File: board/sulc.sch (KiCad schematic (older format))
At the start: 66 parts, among them J1 LED_PWR, J2 HWB, P1 USB, P10 CONN_1, P11 CONN_1, P12 CONN_1, P13 CONN_1, P14 CONN_1, P15 CONN_1, P16 CONN_1, P17 CONN_1, P18 CONN_1, P19 CONN_1, P2 CONN_1, P20 CONN_1, P21 CONN_1, P22 CONN_1, P23 CONN_1, P24 CONN_1, P25 CONN_1, P3 CONN_1, P4 CONN_1, P5 CONN_1, P6 CONN_1, P7 ISP, P8 CONN_1, P9 CONN_1, U1 ATMEGA8U2AU, Y1 16MHz

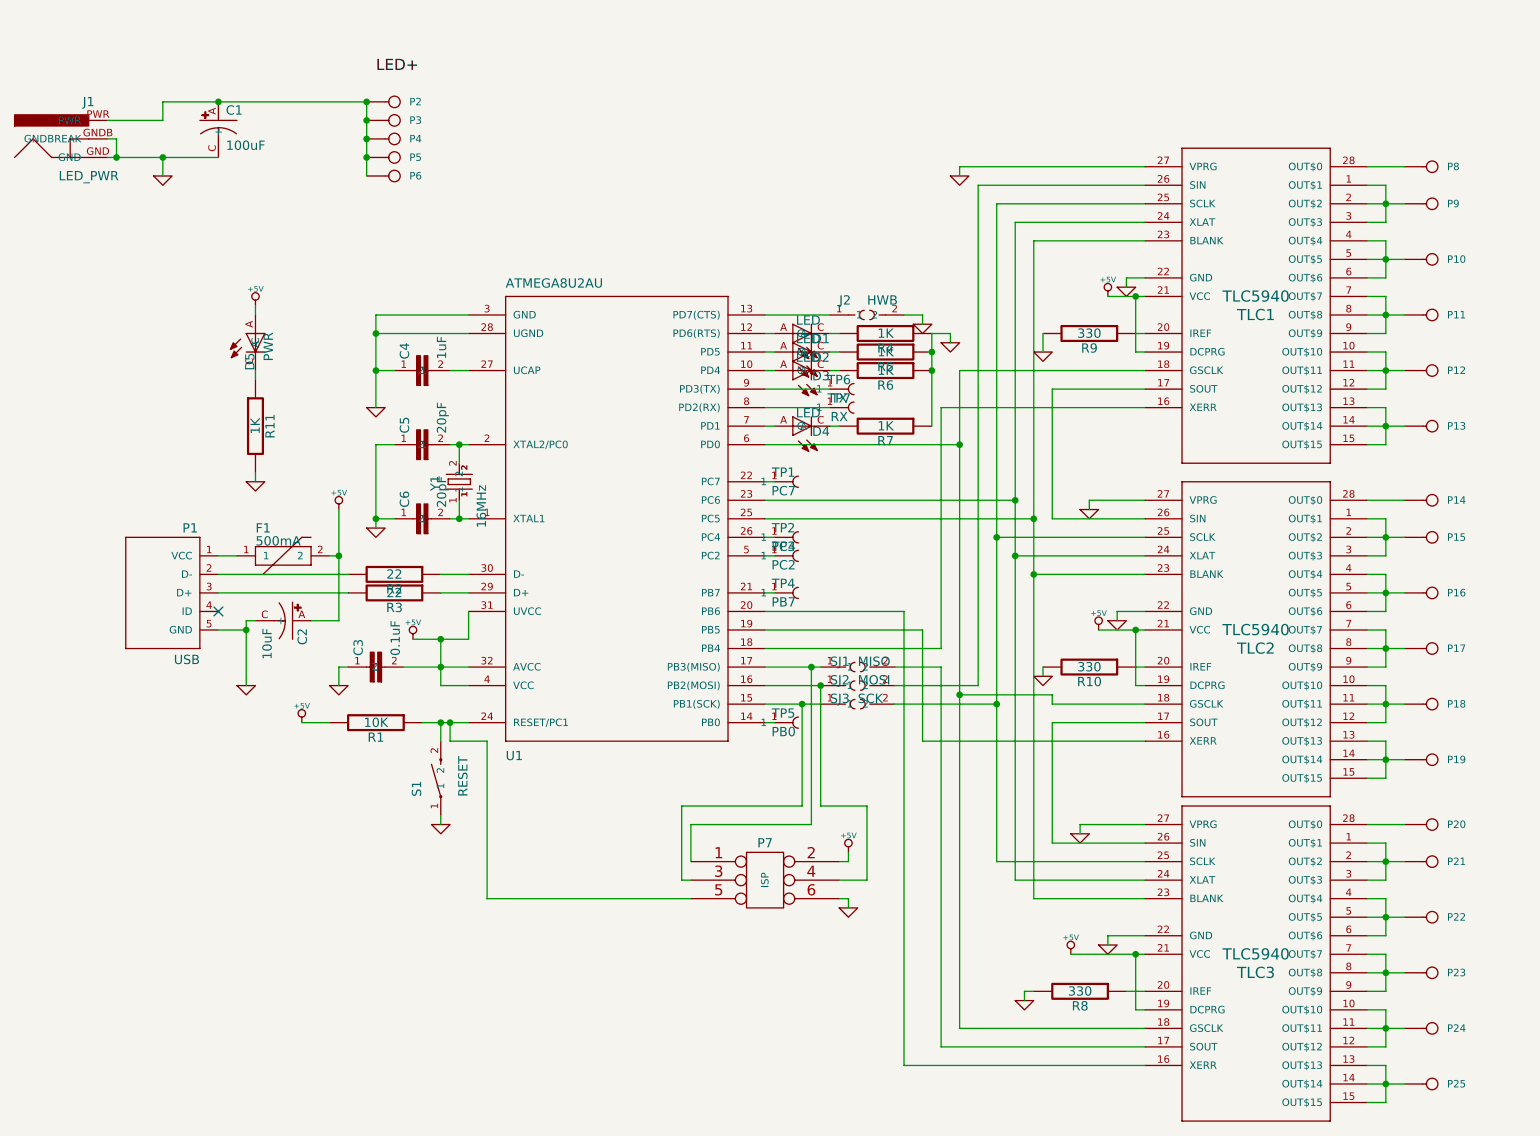
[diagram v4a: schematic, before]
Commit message: Major revision - replaced 1-pin with pin header
- Fixed LED+ and LED pins to be .1" spacing
- Replaced QR code silkscreen with MIT hacker map
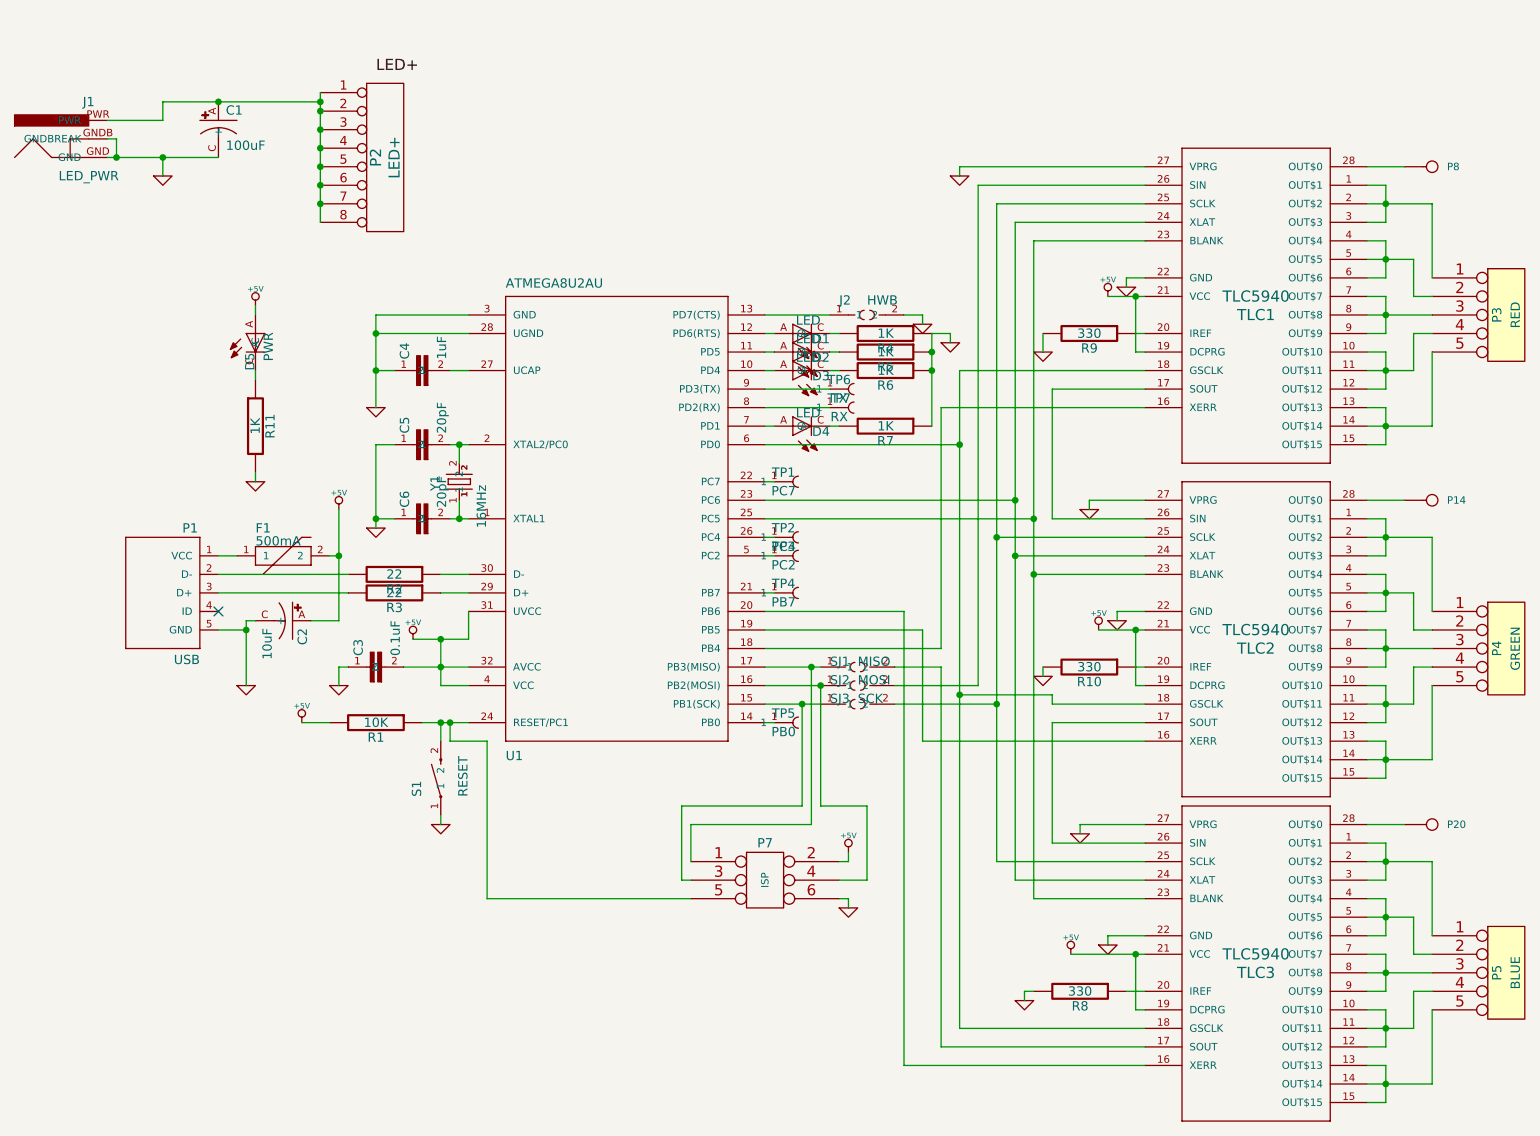
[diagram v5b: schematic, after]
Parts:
- removed P10, P11, P12, P13, P15, P16, P17, P18, P19, P2, P21, P22, P23, P24, P25, P3, P4, P5, P6, P9: CONN_1, symbol CONN_1
- added P2: LED+, symbol CONN_8
- added P3: RED, symbol CONN_5
- added P4: GREEN, symbol CONN_5
- added P5: BLUE, symbol CONN_5
- U1: digikey (none) -> ATMEGA8U2-AU-ND
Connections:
- net at TLC3.1 (OUT$1), TLC3.2 (OUT$2), TLC3.3 (OUT$3): now also P5.1
- net at TLC3.10 (OUT$10), TLC3.11 (OUT$11), TLC3.12 (OUT$12): now also P5.4
- net at TLC3.13 (OUT$13), TLC3.14 (OUT$14), TLC3.15 (OUT$15): now also P5.5
- net at TLC3.4 (OUT$4), TLC3.5 (OUT$5), TLC3.6 (OUT$6): now also P5.2
- net at TLC3.7 (OUT$7), TLC3.8 (OUT$8), TLC3.9 (OUT$9): now also P5.3
- net at TLC2.1 (OUT$1), TLC2.2 (OUT$2), TLC2.3 (OUT$3): now also P4.1
- net at TLC2.10 (OUT$10), TLC2.11 (OUT$11), TLC2.12 (OUT$12): now also P4.4
- net at TLC2.13 (OUT$13), TLC2.14 (OUT$14), TLC2.15 (OUT$15): now also P4.5
- net at TLC2.4 (OUT$4), TLC2.5 (OUT$5), TLC2.6 (OUT$6): now also P4.2
- net at TLC2.7 (OUT$7), TLC2.8 (OUT$8), TLC2.9 (OUT$9): now also P4.3
- net at TLC1.1 (OUT$1), TLC1.2 (OUT$2), TLC1.3 (OUT$3): now also P3.1
- net at TLC1.10 (OUT$10), TLC1.11 (OUT$11), TLC1.12 (OUT$12): now also P3.4
- net at TLC1.13 (OUT$13), TLC1.14 (OUT$14), TLC1.15 (OUT$15): now also P3.5
- net at TLC1.4 (OUT$4), TLC1.5 (OUT$5), TLC1.6 (OUT$6): now also P3.2
- net at TLC1.7 (OUT$7), TLC1.8 (OUT$8), TLC1.9 (OUT$9): now also P3.3
- net at C1.A (+), J1.PWR: now also P2.1 (P1), P2.2 (P2), P2.3 (P3), P2.4 (P4), P2.5 (P5), P2.6 (P6), P2.7 (P7), P2.8 (P8)

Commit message: Added digikey part numbers
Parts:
- C1: digikey (none) -> P833-ND; mfg (none) -> ECE-A1CKA101
- C2: digikey (none) -> P997-ND; mfg (none) -> ECE-A1HKS100
- C3: digikey (none) -> 478-1239-1-ND
- C4: digikey (none) -> 445-1328-1-ND
- C5, C6: digikey (none) -> 445-1272-1-ND
- D1, D2, D3, D4: digikey (none) -> 475-1409-1-ND
- D5: digikey (none) -> 475-2815-1-ND
- J1: digikey (none) -> CP-202A-ND
- P1: digikey (none) -> H2961CT-ND
- P7: digikey (none) -> 609-3218-ND
- R1: digikey (none) -> P10KGCT-ND
- R10, R8, R9: digikey (none) -> P330GCT-ND
- R11, R5, R6, R7: digikey (none) -> P1.0KGCT-ND; mfg (none) -> ERJ-3GEYJ102V
- R2, R3: digikey (none) -> P22GCT-ND
- R4: digikey (none) -> ERJ-3GEYJ102V; mfg (none) -> ERJ-3GEYJ102V
- S1: digikey (none) -> 450-1140-ND
- TLC1, TLC2, TLC3: digikey (none) -> 296-17733-5-ND
- Y1: digikey (none) -> 535-10881-1-ND
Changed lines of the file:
@@
-EESchema Schematic File Version 2  date Monday, February 13, 2012 10:27:21 PM
+EESchema Schematic File Version 2  date Wednesday, February 15, 2012 12:45:44 AM
 LIBS:power
 LIBS:device
@@
 EELAYER 25  0
 EELAYER END
-$Descr A4 11700 8267
+$Descr User 11000 8500
 encoding utf-8
 Sheet 1 1
 Title "SULC - Simple USB LED Controller"
-Date "14 feb 2012"
+Date "15 feb 2012"
 Rev ""
 Comp "Scott Bezek (scottbezek.com)"
@@
 F 1 "PWR" V 2700 2100 50  0000 L BNN
 F 2 "SparkFun-LED-1206" H 2600 2400 50  0001 C CNN
+F 4 "475-2815-1-ND" V 2600 2250 60  0001 C CNN "digikey"
 	1    2600 2250
 	1    0    0    -1
@@
 F 0 "R11" V 2680 2750 50  0000 C CNN
 F 1 "1K" V 2600 2750 50  0000 C CNN
+F 4 "P1.0KGCT-ND" V 2600 2750 60  0001 C CNN "digikey"
+F 5 "ERJ-3GEYJ102V" V 2600 2750 60  0001 C CNN "mfg"
 	1    2600 2750
 	1    0    0    -1
@@
 F 1 "100uF" H 2440 935 50  0000 L BNN
 F 2 "SparkFun-EIA7343" H 2800 850 50  0001 C CNN
+F 4 "P833-ND" H 2400 1100 60  0001 C CNN "digikey"
+F 5 "ECE-A1CKA101" H 2400 1100 60  0001 C CNN "mfg"
 	1    2400 1100
 	1    0    0    -1
@@
 F 1 "LED_PWR" H 1700 1400 50  0000 C CNN
 F 2 "SparkFun-POWER_JACK_PTH" H 1700 1550 50  0001 C CNN
+F 4 "CP-202A-ND" H 1700 1400 60  0001 C CNN "digikey"
 	1    1700 1400
 	1    0    0    -1
@@
 F 1 "10uF" H 2840 3635 50  0000 L BNN
 F 2 "SparkFun-EIA7343" H 3200 3550 50  0001 C CNN
+F 4 "P997-ND" H 2800 3800 60  0001 C CNN "digikey"
+F 5 "ECE-A1HKS100" H 2800 3800 60  0001 C CNN "mfg"
 	1    2800 3800
 	0    1    1    0
@@
 F 1 "0.1uF" H 3360 3965 50  0000 L BNN
 F 2 "SparkFun-1210" H 3650 3900 50  0001 C CNN
+F 4 "478-1239-1-ND" H 3300 4050 60  0001 C CNN "digikey"
 	1    3300 4050
 	0    -1   -1   0
@@
 F 0 "P7" H 5350 5500 50  0000 C CNN
 F 1 "ISP" V 5350 5300 40  0000 C CNN
+F 4 "609-3218-ND" H 5350 5250 60  0001 C CNN "digikey"
 	1    5350 5250
 	1    0    0    -1
@@
 F 0 "R7" V 6080 2750 50  0000 C CNN
 F 1 "1K" V 6000 2750 50  0000 C CNN
+F 4 "P1.0KGCT-ND" V 6000 2750 60  0001 C CNN "digikey"
+F 5 "ERJ-3GEYJ102V" V 6000 2750 60  0001 C CNN "mfg"
 	1    6000 2750
 	0    1    1    0
@@
 F 0 "R6" V 6080 2450 50  0000 C CNN
 F 1 "1K" V 6000 2450 50  0000 C CNN
+F 4 "P1.0KGCT-ND" V 6000 2450 60  0001 C CNN "digikey"
+F 5 "ERJ-3GEYJ102V" V 6000 2450 60  0001 C CNN "mfg"
 	1    6000 2450
 	0    1    1    0
@@
 F 0 "R5" V 6080 2350 50  0000 C CNN
 F 1 "1K" V 6000 2350 50  0000 C CNN
+F 4 "P1.0KGCT-ND" V 6000 2350 60  0001 C CNN "digikey"
+F 5 "ERJ-3GEYJ102V" V 6000 2350 60  0001 C CNN "mfg"
 	1    6000 2350
 	0    1    1    0
@@
 F 0 "R4" V 6080 2250 50  0000 C CNN
 F 1 "1K" V 6000 2250 50  0000 C CNN
+F 4 "ERJ-3GEYJ102V" V 6000 2250 60  0001 C CNN "digikey"
+F 5 "ERJ-3GEYJ102V" V 6000 2250 60  0001 C CNN "mfg"
 	1    6000 2250
 	0    1    1    0
@@
 F 1 "LED" V 5600 2100 50  0000 L BNN
 F 2 "SparkFun-LED-1206" H 5500 2400 50  0001 C CNN
+F 4 "475-1409-1-ND" V 5500 2250 60  0001 C CNN "digikey"
 	1    5500 2250
 	0    -1   -1   0
@@
 F 1 "LED" V 5600 2200 50  0000 L BNN
 F 2 "SparkFun-LED-1206" H 5500 2500 50  0001 C CNN
+F 4 "475-1409-1-ND" V 5500 2350 60  0001 C CNN "digikey"
 	1    5500 2350
 	0    -1   -1   0
@@
 F 1 "LED" V 5600 2300 50  0000 L BNN
 F 2 "SparkFun-LED-1206" H 5500 2600 50  0001 C CNN
+F 4 "475-1409-1-ND" V 5500 2450 60  0001 C CNN "digikey"
 	1    5500 2450
 	0    -1   -1   0
@@
 F 1 "LED" V 5600 2600 50  0000 L BNN
 F 2 "SparkFun-LED-1206" H 5500 2900 50  0001 C CNN
+F 4 "475-1409-1-ND" V 5500 2750 60  0001 C CNN "digikey"
 	1    5500 2750
 	0    -1   -1   0
@@
 F 0 "R8" V 7130 5800 50  0000 C CNN
 F 1 "330" V 7050 5800 50  0000 C CNN
+F 4 "P330GCT-ND" V 7050 5800 60  0001 C CNN "digikey"
 	1    7050 5800
 	0    1    1    0
@@
 F 0 "R10" V 7180 4050 50  0000 C CNN
 F 1 "330" V 7100 4050 50  0000 C CNN
+F 4 "P330GCT-ND" V 7100 4050 60  0001 C CNN "digikey"
 	1    7100 4050
 	0    1    1    0
@@
 F 0 "R9" V 7180 2250 50  0000 C CNN
 F 1 "330" V 7100 2250 50  0000 C CNN
+F 4 "P330GCT-ND" V 7100 2250 60  0001 C CNN "digikey"
 	1    7100 2250
 	0    1    1    0
@@
 F 0 "R1" V 3330 4350 50  0000 C CNN
 F 1 "10K" V 3250 4350 50  0000 C CNN
+F 4 "P10KGCT-ND" V 3250 4350 60  0001 C CNN "digikey"
 	1    3250 4350
 	0    1    1    0
@@
 F 1 "RESET" H 3500 4500 50  0000 L BNN
 F 2 "SparkFun-TACTILE-SWITCH-1101NE" H 4200 4450 50  0001 C CNN
+F 4 "450-1140-ND" H 3600 4650 60  0001 C CNN "digikey"
 	1    3600 4650
 	0    -1   -1   0
@@
 F 0 "TLC3" H 8000 5500 60  0000 C CNN
 F 1 "TLC5940" H 8000 5600 60  0000 C CNN
+F 4 "296-17733-5-ND" H 8000 5600 60  0001 C CNN "digikey"
 	1    8000 5600
 	-1   0    0    -1
@@
 F 0 "TLC2" H 8000 3750 60  0000 C CNN
 F 1 "TLC5940" H 8000 3850 60  0000 C CNN
+F 4 "296-17733-5-ND" H 8000 3850 60  0001 C CNN "digikey"
 	1    8000 3850
 	-1   0    0    -1
@@
 F 0 "TLC1" H 8000 1950 60  0000 C CNN
 F 1 "TLC5940" H 8000 2050 60  0000 C CNN
+F 4 "296-17733-5-ND" H 8000 2050 60  0001 C CNN "digikey"
 	1    8000 2050
 	-1   0    0    -1
@@
 F 1 "20pF" H 3610 3165 50  0000 L BNN
 F 2 "SparkFun-1210" H 3900 3100 50  0001 C CNN
+F 4 "445-1272-1-ND" H 3550 3250 60  0001 C CNN "digikey"
 	1    3550 3250
 	0    -1   -1   0
@@
 F 1 "20pF" H 3610 2765 50  0000 L BNN
 F 2 "SparkFun-1210" H 3900 2700 50  0001 C CNN
+F 4 "445-1272-1-ND" H 3550 2850 60  0001 C CNN "digikey"
 	1    3550 2850
 	0    -1   -1   0
@@
 F 1 "16MHz" H 3450 2900 50  0000 L BNN
 F 2 "SparkFun-HC49UP" H 3700 2850 50  0001 C CNN
+F 4 "535-10881-1-ND" H 3700 3050 60  0001 C CNN "digikey"
 	1    3700 3050
 	0    -1   -1   0
@@
 F 1 "1uF" H 3610 2365 50  0000 L BNN
 F 2 "SparkFun-1210" H 3900 2300 50  0001 C CNN
+F 4 "445-1328-1-ND" H 3550 2450 60  0001 C CNN "digikey"
 	1    3550 2450
 	0    -1   -1   0
@@
 F 0 "R2" V 3430 3550 50  0000 C CNN
 F 1 "22" V 3350 3550 50  0000 C CNN
+F 4 "P22GCT-ND" V 3350 3550 60  0001 C CNN "digikey"
 	1    3350 3550
 	0    1    1    0
@@
 F 0 "R3" V 3430 3650 50  0000 C CNN
 F 1 "22" V 3350 3650 50  0000 C CNN
+F 4 "P22GCT-ND" V 3350 3650 60  0001 C CNN "digikey"
 	1    3350 3650
 	0    1    1    0
@@
 F 1 "USB" H 1900 3260 50  0000 L BNN
 F 2 "SparkFun-MICRO-B-SMT" H 2100 3800 50  0001 C CNN
+F 4 "H2961CT-ND" H 2100 3650 60  0001 C CNN "digikey"
 	1    2100 3650
 	-1   0    0    -1

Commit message: Major revision - fixed TLC5940 pinout
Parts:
- removed TLC1, TLC2, TLC3: TLC5940, symbol TLC5940
- added TLC1, TLC2, TLC3: TLC5940_TSSOP, symbol TLC5940_TSSOP
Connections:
- net labels added: BLANK, GSCLK, L1_1, L1_2, L1_3, L1_4, L1_5, L2_1, L2_2, L2_3, L2_4, L2_5, L3_1, L3_2, L3_3, L3_4, L3_5, LED_PWR, MOSI_SIN, RESET, SCLK, SOUT1_SIN2, SOUT2_SIN3, SOUT3_MISO, XERR1, XERR2, XERR3, XLAT
- wire segments 240 -> 243

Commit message: Added BLANK pullup. fixes #2
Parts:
- added R?: 10K, symbol R
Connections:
- wire segments 243 -> 244
